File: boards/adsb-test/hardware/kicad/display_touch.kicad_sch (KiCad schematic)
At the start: 0 parts

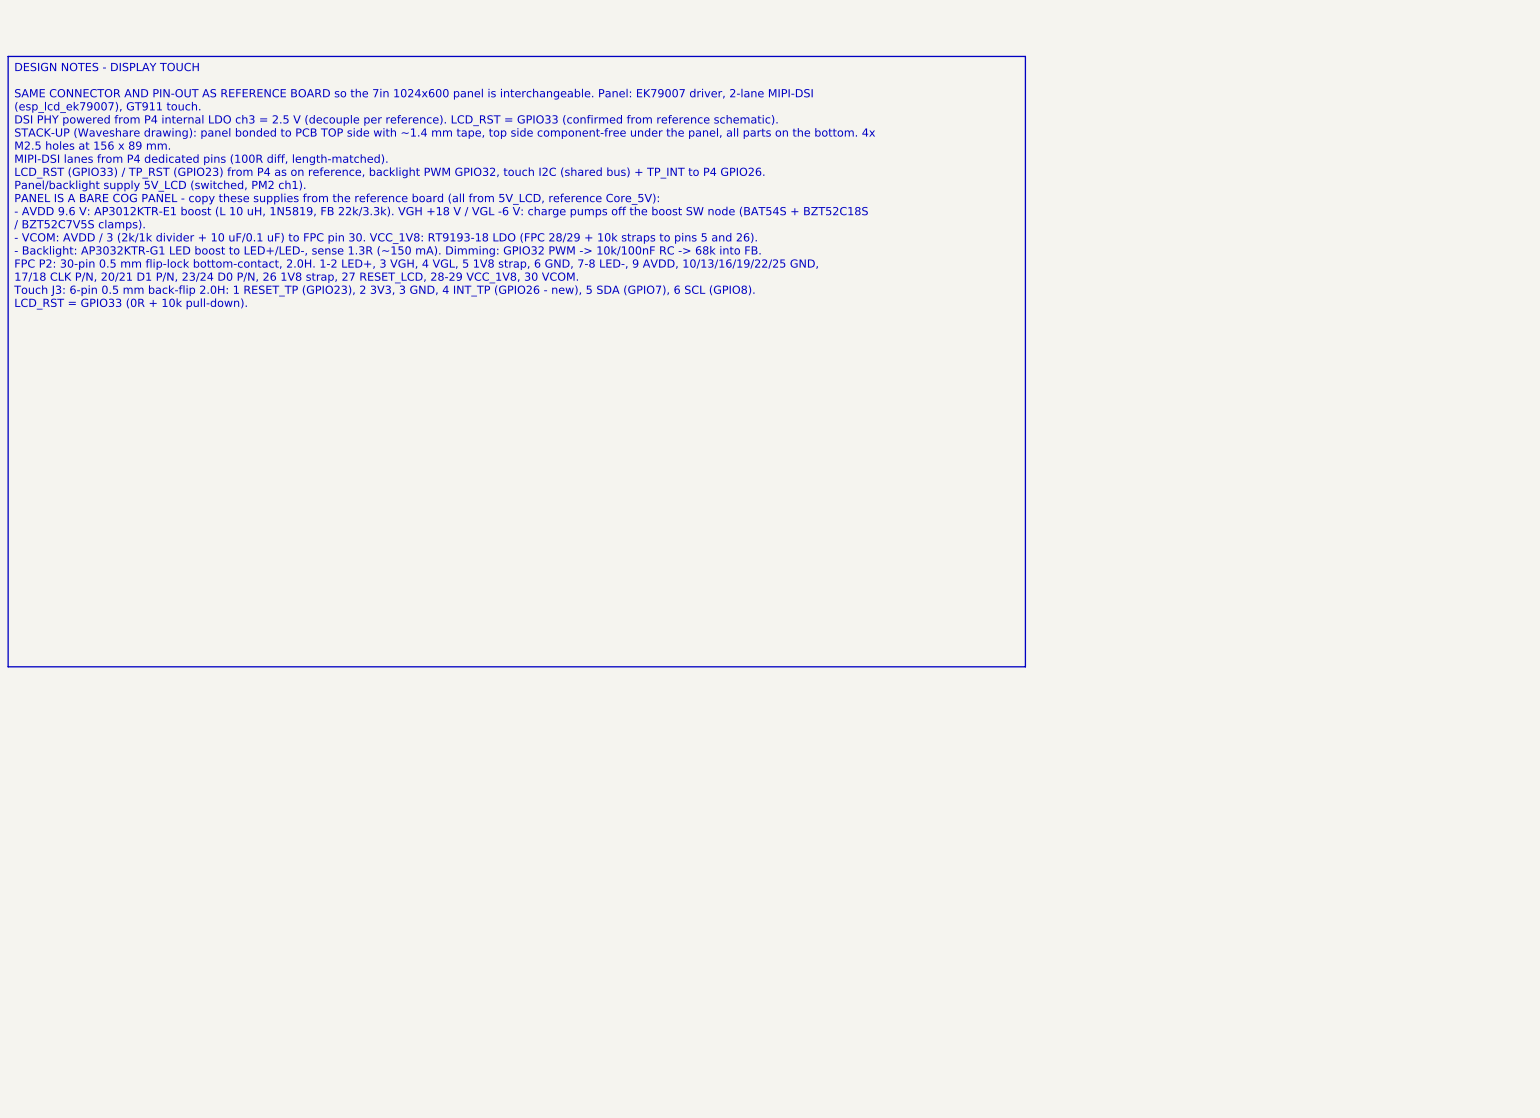
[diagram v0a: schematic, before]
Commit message: Release v0.22.0: all ADSB_Test schematic sheets generated (ERC clean)
Co-Authored-By: Claude Opus 5.5 <noreply@anthropic.com>
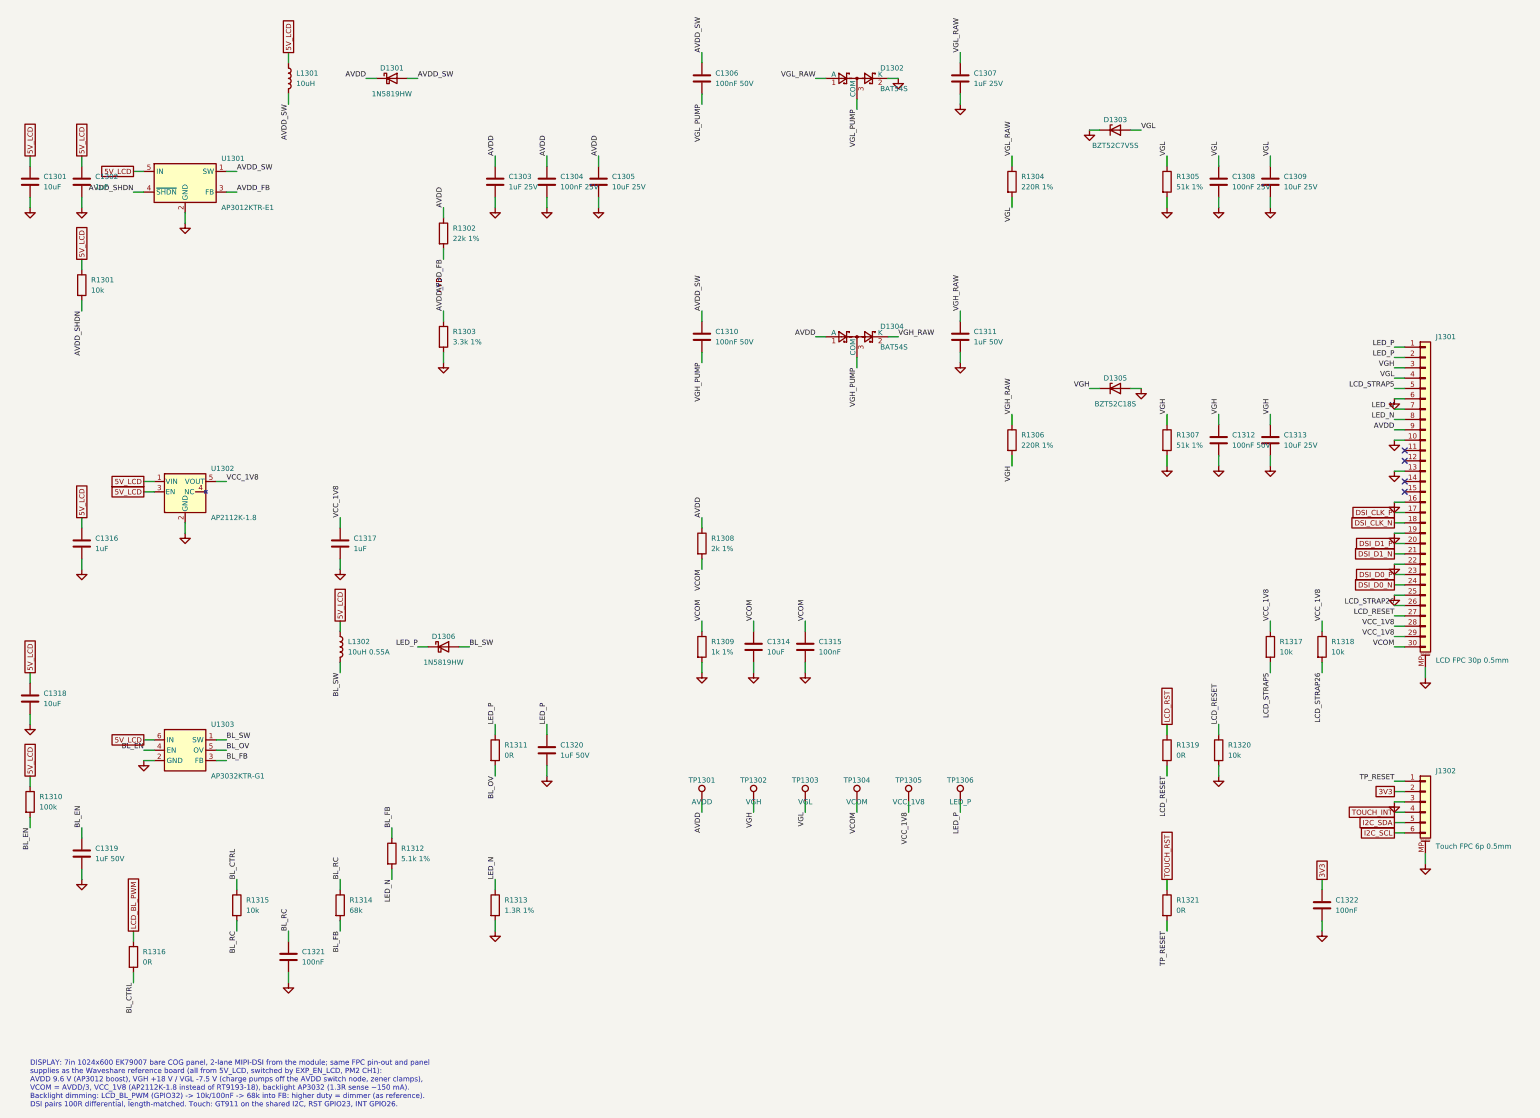
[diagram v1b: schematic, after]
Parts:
- added C1301, C1314, C1318: 10uF, Capacitor_SMD:C_1206_3216Metric_Pad1.33x1.80mm_HandSolder, symbol Device:C
- added C1302, C1316, C1317: 1uF, Capacitor_SMD:C_0805_2012Metric_Pad1.18x1.45mm_HandSolder, symbol Device:C
- added C1303, C1307: 1uF 25V, Capacitor_SMD:C_0805_2012Metric_Pad1.18x1.45mm_HandSolder, symbol Device:C
- added C1304, C1308: 100nF 25V, Capacitor_SMD:C_0805_2012Metric_Pad1.18x1.45mm_HandSolder, symbol Device:C
- added C1305, C1309, C1313: 10uF 25V, Capacitor_SMD:C_1206_3216Metric_Pad1.33x1.80mm_HandSolder, symbol Device:C
- added C1306, C1310, C1312: 100nF 50V, Capacitor_SMD:C_0805_2012Metric_Pad1.18x1.45mm_HandSolder, symbol Device:C
- added C1311: 1uF 50V, Capacitor_SMD:C_0805_2012Metric_Pad1.18x1.45mm_HandSolder, symbol Device:C
- added C1315, C1321, C1322: 100nF, Capacitor_SMD:C_0805_2012Metric_Pad1.18x1.45mm_HandSolder, symbol Device:C
- added C1319, C1320: 1uF 50V, Capacitor_SMD:C_1206_3216Metric_Pad1.33x1.80mm_HandSolder, symbol Device:C
- added D1301, D1306: 1N5819HW, Diode_SMD:D_SOD-123, symbol Device:D_Schottky
- added D1302, D1304: BAT54S, Package_TO_SOT_SMD:SOT-23_Handsoldering, symbol Diode:BAT54S
- added D1303: BZT52C7V5S, Diode_SMD:D_SOD-123F, symbol Diode:BZT52Bxx
- added D1305: BZT52C18S, Diode_SMD:D_SOD-123F, symbol Diode:BZT52Bxx
- added J1301: LCD FPC 30p 0.5mm, Connector_FFC-FPC:Hirose_FH12-30S-0.5SH_1x30-1MP_P0.50mm_Horizontal, symbol Connector_Generic_MountingPin:Conn_01x30_MountingPin
- added J1302: Touch FPC 6p 0.5mm, Connector_FFC-FPC:Hirose_FH12-6S-0.5SH_1x06-1MP_P0.50mm_Horizontal, symbol Connector_Generic_MountingPin:Conn_01x06_MountingPin
- added L1301: 10uH, Inductor_SMD:L_Bourns-SRN4018, symbol Device:L
- added L1302: 10uH 0.55A, Inductor_SMD:L_Bourns-SRN4018, symbol Device:L
- added R1301, R1315, R1317, R1318, R1320: 10k, Resistor_SMD:R_0805_2012Metric_Pad1.20x1.40mm_HandSolder, symbol Device:R
- added R1302: 22k 1%, Resistor_SMD:R_0805_2012Metric_Pad1.20x1.40mm_HandSolder, symbol Device:R
- added R1303: 3.3k 1%, Resistor_SMD:R_0805_2012Metric_Pad1.20x1.40mm_HandSolder, symbol Device:R
- added R1304, R1306: 220R 1%, Resistor_SMD:R_0805_2012Metric_Pad1.20x1.40mm_HandSolder, symbol Device:R
- added R1305, R1307: 51k 1%, Resistor_SMD:R_0805_2012Metric_Pad1.20x1.40mm_HandSolder, symbol Device:R
- added R1308: 2k 1%, Resistor_SMD:R_0805_2012Metric_Pad1.20x1.40mm_HandSolder, symbol Device:R
- added R1309: 1k 1%, Resistor_SMD:R_0805_2012Metric_Pad1.20x1.40mm_HandSolder, symbol Device:R
- added R1310: 100k, Resistor_SMD:R_0805_2012Metric_Pad1.20x1.40mm_HandSolder, symbol Device:R
- added R1311, R1316, R1319, R1321: 0R, Resistor_SMD:R_0805_2012Metric_Pad1.20x1.40mm_HandSolder, symbol Device:R
- added R1312: 5.1k 1%, Resistor_SMD:R_0805_2012Metric_Pad1.20x1.40mm_HandSolder, symbol Device:R
- added R1313: 1.3R 1%, Resistor_SMD:R_1206_3216Metric_Pad1.30x1.75mm_HandSolder, symbol Device:R
- added R1314: 68k, Resistor_SMD:R_0805_2012Metric_Pad1.20x1.40mm_HandSolder, symbol Device:R
- added TP1301: AVDD, TestPoint:TestPoint_Pad_D1.5mm, symbol Connector:TestPoint
- added TP1302: VGH, TestPoint:TestPoint_Pad_D1.5mm, symbol Connector:TestPoint
- added TP1303: VGL, TestPoint:TestPoint_Pad_D1.5mm, symbol Connector:TestPoint
- added TP1304: VCOM, TestPoint:TestPoint_Pad_D1.5mm, symbol Connector:TestPoint
- added TP1305: VCC_1V8, TestPoint:TestPoint_Pad_D1.5mm, symbol Connector:TestPoint
- added TP1306: LED_P, TestPoint:TestPoint_Pad_D1.5mm, symbol Connector:TestPoint
- added U1301: AP3012KTR-E1, Package_TO_SOT_SMD:SOT-23-5_HandSoldering, symbol Regulator_Switching:AP3012
- added U1302: AP2112K-1.8, Package_TO_SOT_SMD:SOT-23-5_HandSoldering, symbol Regulator_Linear:AP2112K-1.8
- added U1303: AP3032KTR-G1, Package_TO_SOT_SMD:SOT-23-6_Handsoldering, symbol ADSB_Test:AP3032
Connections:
- new net 3V3: C1322.1, J1302.2 (Pin_2)
- new net 5V_LCD: C1301.1, C1302.1, C1316.1, C1318.1, L1301.1, L1302.1, R1301.1, R1310.1, U1301.5 (IN), U1302.1 (VIN), U1302.3 (EN), U1303.6 (IN)
- new net AVDD: C1303.1, C1304.1, C1305.1, D1301.1 (K), D1304.1 (A), J1301.9 (Pin_9), R1302.1, R1308.1, TP1301.1
- new net AVDD_FB: R1302.2, R1303.1, U1301.3 (FB)
- new net AVDD_SHDN: R1301.2, U1301.4 (~{SHDN})
- new net AVDD_SW: C1306.1, C1310.1, D1301.2 (A), L1301.2, U1301.1 (SW)
- new net BL_CTRL: R1315.1, R1316.2
- new net BL_EN: C1319.1, R1310.2, U1303.4 (EN)
- new net BL_FB: R1312.1, R1314.2, U1303.3 (FB)
- new net BL_OV: R1311.2, U1303.5 (OV)
- new net BL_RC: C1321.1, R1314.1, R1315.2
- new net BL_SW: D1306.2 (A), L1302.2, U1303.1 (SW)
- new net DSI_CLK_N: J1301.18 (Pin_18)
- new net DSI_CLK_P: J1301.17 (Pin_17)
- new net DSI_D0_N: J1301.24 (Pin_24)
- new net DSI_D0_P: J1301.23 (Pin_23)
- new net DSI_D1_N: J1301.21 (Pin_21)
- new net DSI_D1_P: J1301.20 (Pin_20)
- new net GND: C1301.2, C1302.2, C1303.2, C1304.2, C1305.2, C1307.2, C1308.2, C1309.2, C1311.2, C1312.2, C1313.2, C1314.2, C1315.2, C1316.2, C1317.2, C1318.2, C1319.2, C1320.2, C1321.2, C1322.2, D1302.2 (K), D1303.1 (K), D1305.2 (A), J1301.10 (Pin_10), J1301.13 (Pin_13), J1301.16 (Pin_16), J1301.19 (Pin_19), J1301.22 (Pin_22), J1301.25 (Pin_25), J1301.6 (Pin_6), J1301.MP (MountPin), J1302.3 (Pin_3), J1302.MP (MountPin), R1303.2, R1305.2, R1307.2, R1309.2, R1313.2, R1320.2, U1301.2 (GND), U1302.2 (GND), U1303.2 (GND)
- new net I2C_SCL: J1302.6 (Pin_6)
- new net I2C_SDA: J1302.5 (Pin_5)
- new net LCD_BL_PWM: R1316.1
- new net LCD_RESET: J1301.27 (Pin_27), R1319.2, R1320.1
- new net LCD_RST: R1319.1
- new net LCD_STRAP26: J1301.26 (Pin_26), R1318.2
- new net LCD_STRAP5: J1301.5 (Pin_5), R1317.2
- new net LED_N: J1301.7 (Pin_7), J1301.8 (Pin_8), R1312.2, R1313.1
- new net LED_P: C1320.1, D1306.1 (K), J1301.1 (Pin_1), J1301.2 (Pin_2), R1311.1, TP1306.1
- new net TOUCH_INT: J1302.4 (Pin_4)
- new net TOUCH_RST: R1321.1
- new net TP_RESET: J1302.1 (Pin_1), R1321.2
- new net VCC_1V8: C1317.1, J1301.28 (Pin_28), J1301.29 (Pin_29), R1317.1, R1318.1, TP1305.1, U1302.5 (VOUT)
- new net VCOM: C1314.1, C1315.1, J1301.30 (Pin_30), R1308.2, R1309.1, TP1304.1
- new net VGH: C1312.1, C1313.1, D1305.1 (K), J1301.3 (Pin_3), R1306.2, R1307.1, TP1302.1
- new net VGH_PUMP: C1310.2, D1304.3 (COM)
- new net VGH_RAW: C1311.1, D1304.2 (K), R1306.1
- new net VGL: C1308.1, C1309.1, D1303.2 (A), J1301.4 (Pin_4), R1304.2, R1305.1, TP1303.1
- new net VGL_PUMP: C1306.2, D1302.3 (COM)
- new net VGL_RAW: C1307.1, D1302.1 (A), R1304.1
- no-connect marks 0 -> 4
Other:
- note added: "DISPLAY: 7in 1024x600 EK79007 bare COG panel, 2-lane MIPI-DSI from the module; same FPC pin-out and panel supplies as the Waveshare reference board (all from 5V_LCD, switched by EXP_EN_LCD, PM2 CH1): AVDD 9.6 V (AP3012 boost), VGH +18 V / VGL -7.5 V (charge pumps off the AVDD switch node, zener clamps), VCOM = AVDD/3, VCC_1V8 (AP2112K-1.8 instead of RT9193-18), backlight AP3032 (1.3R sense ~150 m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"

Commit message: ADSB_Test display: scan-direction strap options on FPC pins 5/6
Co-Authored-By: Claude Opus 5.5 <noreply@anthropic.com>
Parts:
- added R1322, R1323: 0R, Resistor_SMD:R_0805_2012Metric_Pad1.20x1.40mm_HandSolder, symbol Device:R
- added R1324: 10k, Resistor_SMD:R_0805_2012Metric_Pad1.20x1.40mm_HandSolder, symbol Device:R
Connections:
- net GND: now also R1322.2, R1323.2; no longer J1301.6 (Pin_6)
- net LCD_STRAP5: now also R1322.1
- net VCC_1V8: now also R1324.1
- new net LCD_STRAP6: J1301.6 (Pin_6), R1323.1, R1324.2

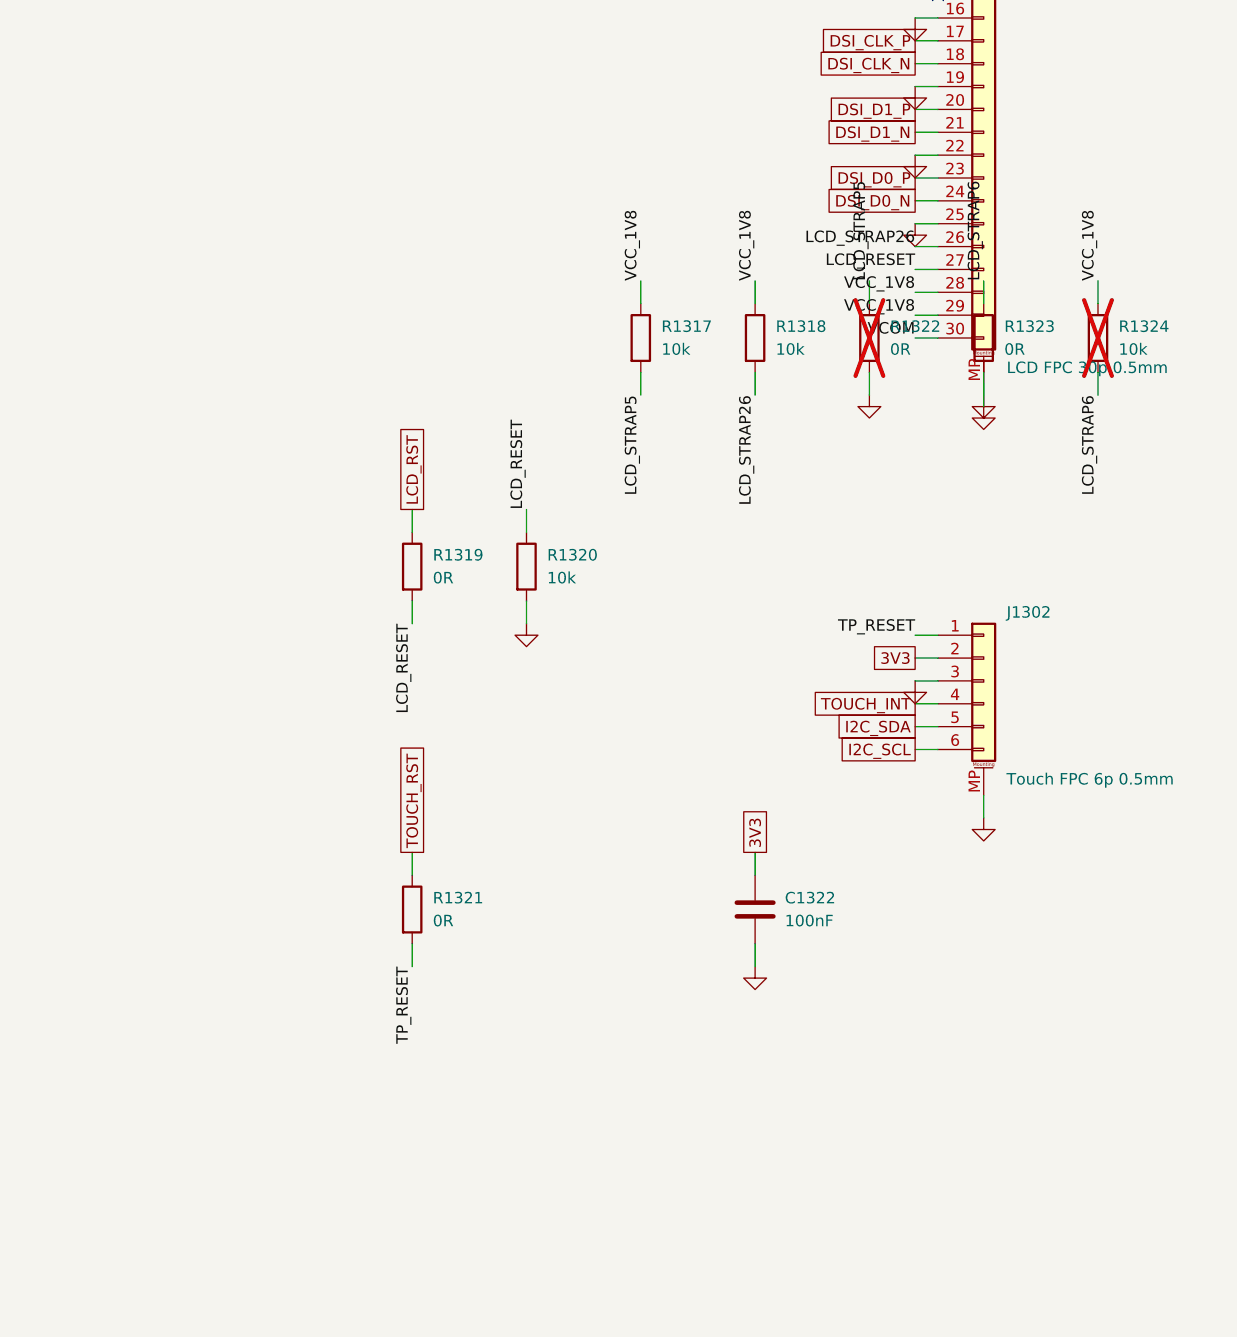
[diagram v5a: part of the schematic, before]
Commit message: ADSB_Test display sheet: move LCD strap resistors off the FPC connector
Co-Authored-By: Claude Opus 5.5 <noreply@anthropic.com>
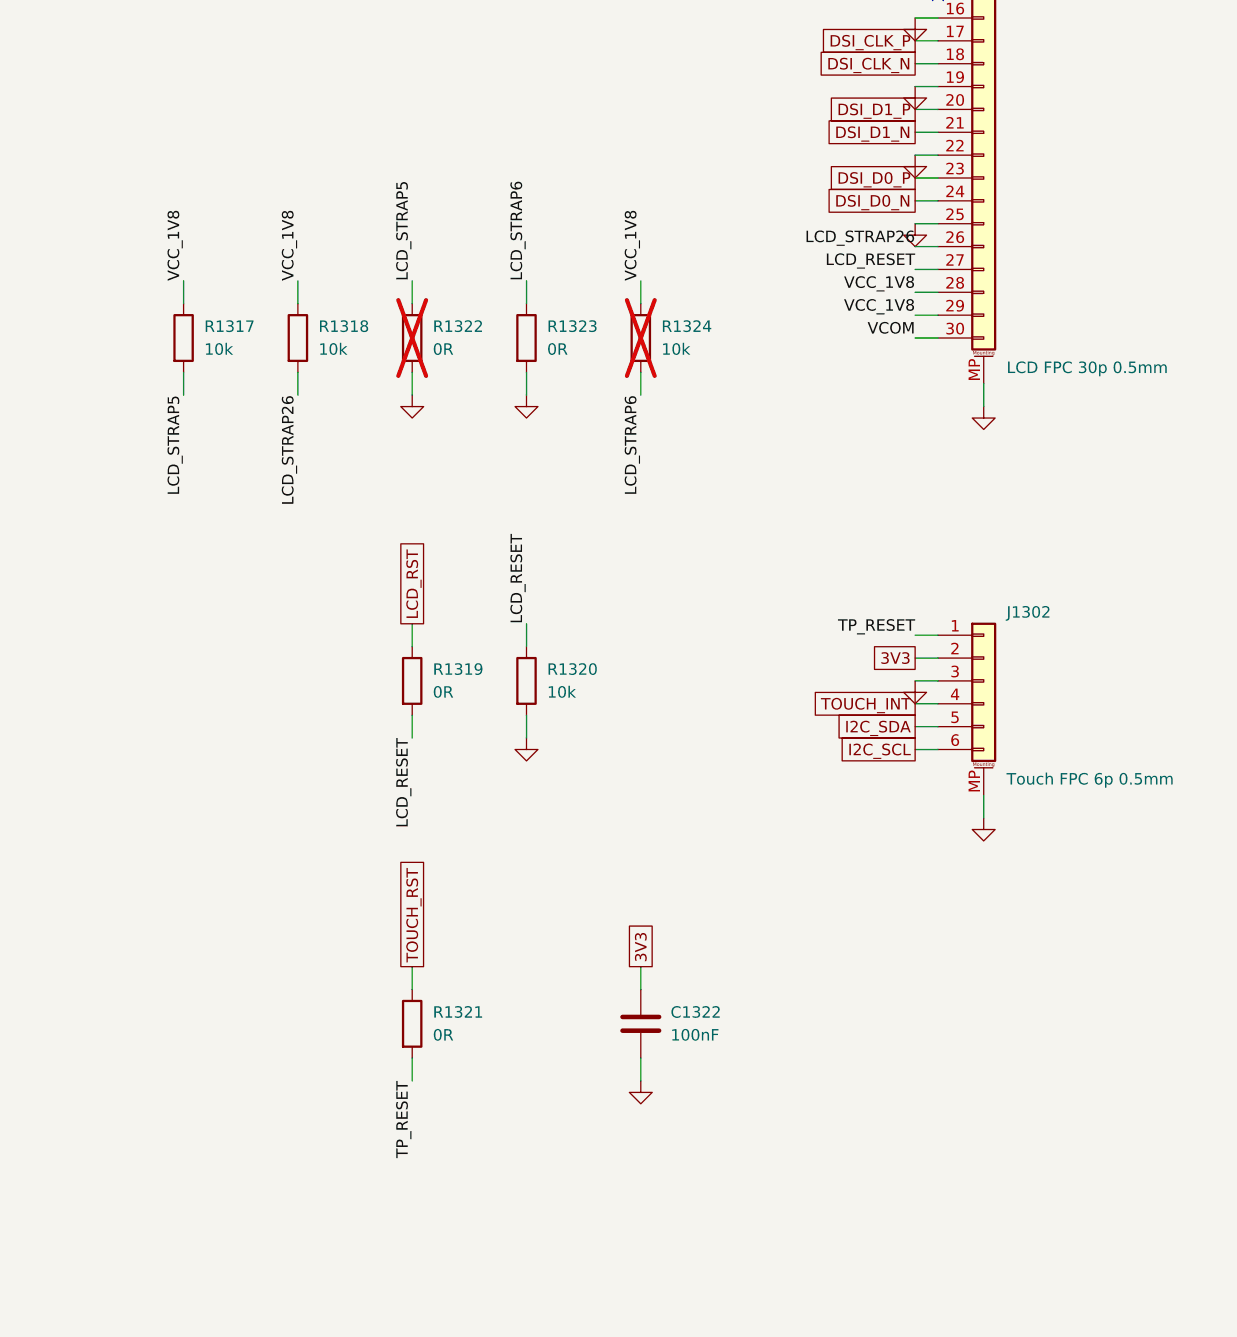
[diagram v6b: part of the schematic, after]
